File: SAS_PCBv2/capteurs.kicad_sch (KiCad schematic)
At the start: 8 parts, among them J1 BMP280, J12 Conn_01x04, Q4 BS170, Q5 BS170

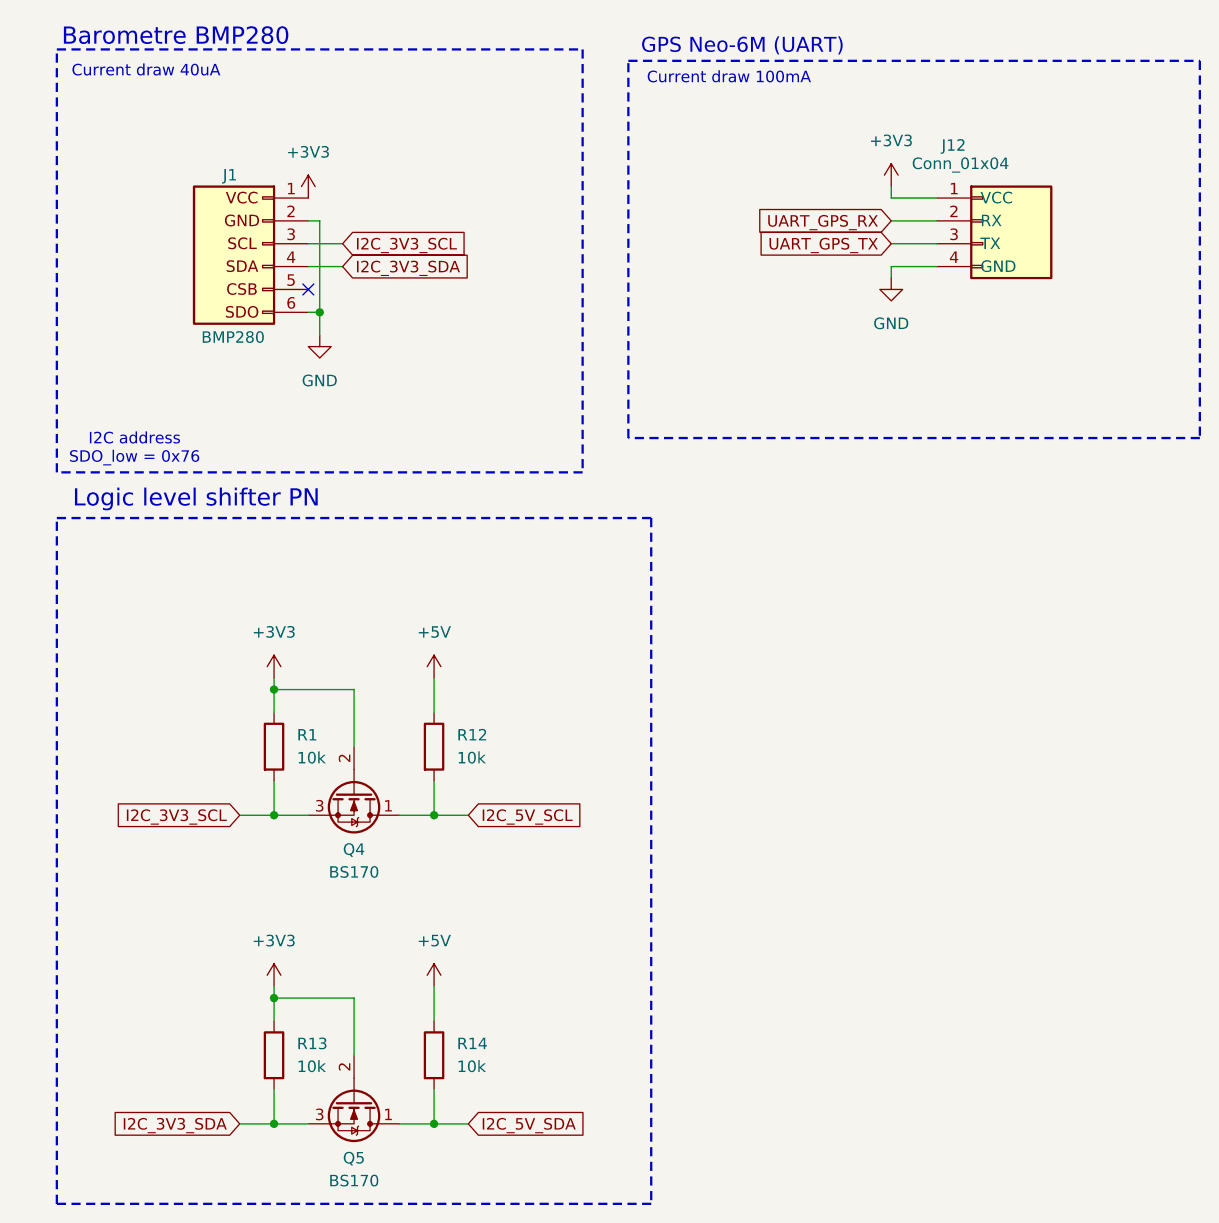
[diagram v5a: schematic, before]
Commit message: Identification des transistors, footprint BMP280 et GPS Neo-6M, correction du fan PWM
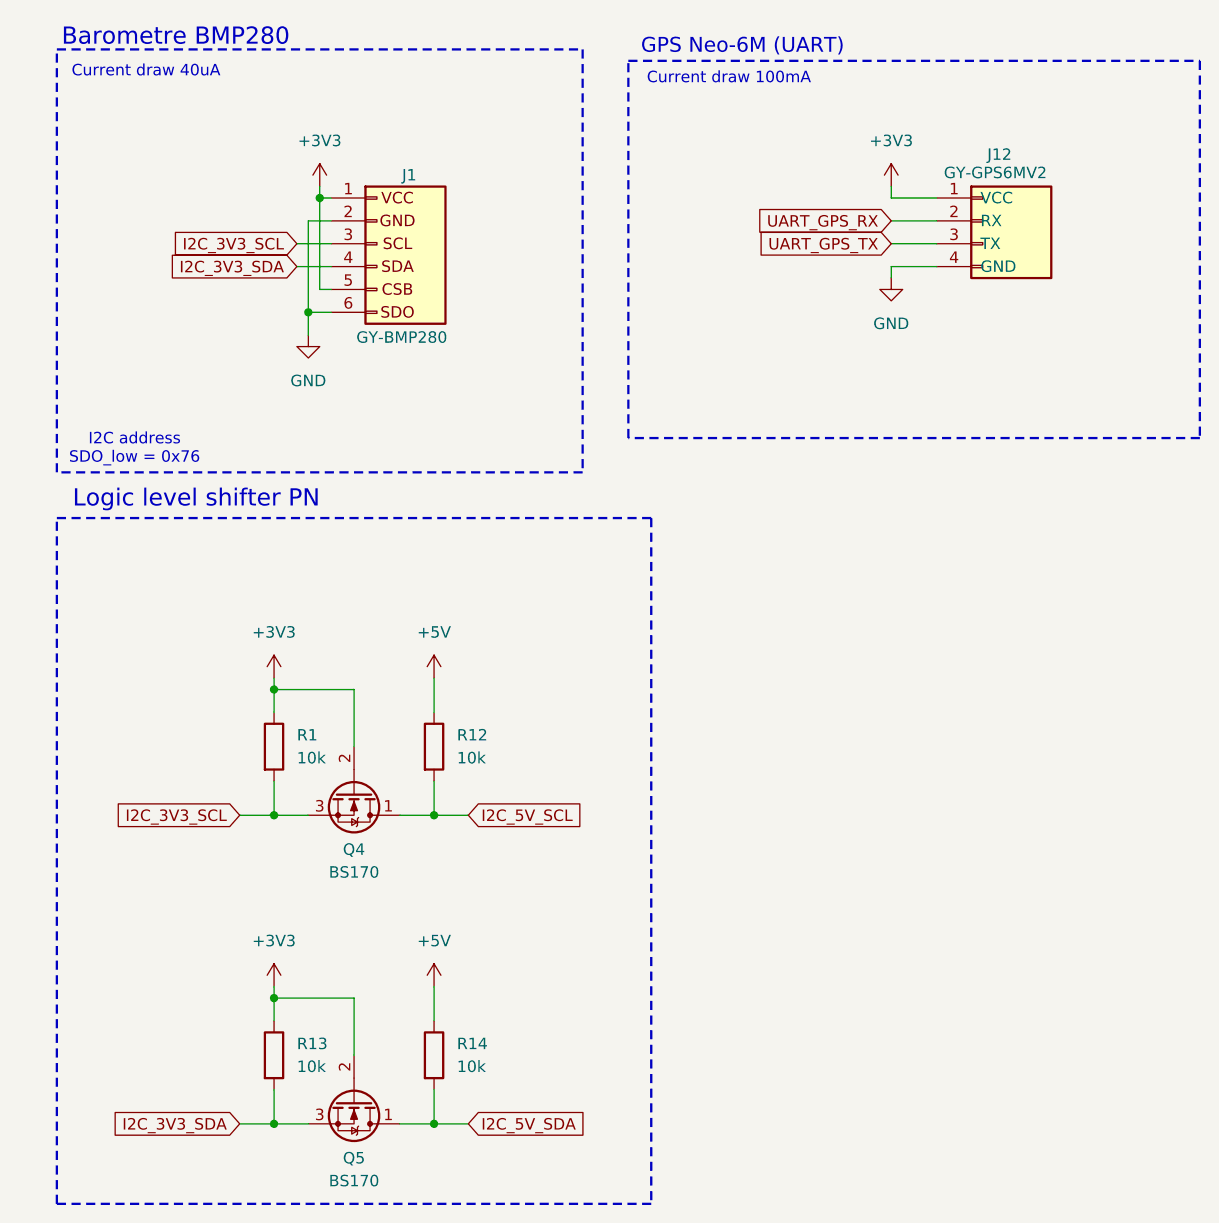
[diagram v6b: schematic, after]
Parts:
- J1: value BMP280 -> GY-BMP280
- J12: value Conn_01x04 -> GY-GPS6MV2
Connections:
- net +3V3: now also J1.5 (Pin_5)
- no-connect marks 1 -> 0
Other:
- moved on the sheet: J1
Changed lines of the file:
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@@
+	)
+	(junction
+		(at 43.18 46.99)
+		(diameter 0)
+		(color 0 0 0 0)
 	)
 	(junction
@@
 	)
 	(junction
+		(at 44.45 34.29)
+		(diameter 0)
+		(color 0 0 0 0)
+	)
+	(junction
 		(at 39.37 123.19)
 		(diameter 0)
@@
 		(color 0 0 0 0)
 	)
-	(junction
-		(at 44.45 46.99)
-		(diameter 0)
-		(color 0 0 0 0)
-	)
-	(no_connect
-		(at 43.18 44.45)
-	)
 	(wire
 		(pts
@@
 	(wire
 		(pts
+			(xy 44.45 34.29) (xy 45.72 34.29)
+		)
+		(stroke
+			(width 0)
+			(type default)
+		)
+	)
+	(wire
+		(pts
 			(xy 48.26 129.54) (xy 48.26 123.19)
 		)
@@
 	(wire
 		(pts
+			(xy 44.45 34.29) (xy 44.45 44.45)
+		)
+		(stroke
+			(width 0)
+			(type default)
+		)
+	)
+	(wire
+		(pts
 			(xy 107.95 39.37) (xy 113.03 39.37)
 		)
@@
 	(wire
 		(pts
-			(xy 43.18 41.91) (xy 46.99 41.91)
+			(xy 45.72 41.91) (xy 41.91 41.91)
 		)
 		(stroke
@@
 	(wire
 		(pts
-			(xy 44.45 46.99) (xy 44.45 49.53)
-		)
-		(stroke
-			(width 0)
-			(type default)
-		)
-	)
-	(wire
-		(pts
-			(xy 44.45 36.83) (xy 43.18 36.83)
+			(xy 43.18 46.99) (xy 43.18 49.53)
+		)
+		(stroke
+			(width 0)
+			(type default)
+		)
+	)
+	(wire
+		(pts
+			(xy 43.18 36.83) (xy 45.72 36.83)
 		)
 		(stroke
@@
 	(wire
 		(pts
+			(xy 45.72 44.45) (xy 44.45 44.45)
+		)
+		(stroke
+			(width 0)
+			(type default)
+		)
+	)
+	(wire
+		(pts
 			(xy 39.37 102.87) (xy 43.18 102.87)
 		)
@@
 	(wire
 		(pts
+			(xy 44.45 33.02) (xy 44.45 34.29)
+		)
+		(stroke
+			(width 0)
+			(type default)
+		)
+	)
+	(wire
+		(pts
 			(xy 39.37 133.35) (xy 39.37 137.16)
 		)
@@
 	(wire
 		(pts
-			(xy 43.18 46.99) (xy 44.45 46.99)
+			(xy 43.18 46.99) (xy 45.72 46.99)
 		)
 		(stroke
@@
 	(wire
 		(pts
-			(xy 44.45 36.83) (xy 44.45 46.99)
+			(xy 43.18 36.83) (xy 43.18 46.99)
 		)
 		(stroke
@@
 	(wire
 		(pts
-			(xy 43.18 39.37) (xy 46.99 39.37)
+			(xy 45.72 39.37) (xy 41.91 39.37)
 		)
 		(stroke
@@
 	(global_label "I2C_3V3_SDA"
 		(shape input)
-		(at 46.99 41.91 0)
+		(at 41.91 41.91 180)
 		(fields_autoplaced yes)
 		(effects
@@
 				(size 1.27 1.27)
 			)
-			(justify left)
+			(justify right)
 		)
 		(property "Intersheetrefs" "${INTERSHEET_REFS}"
-			(at 62.0704 41.91 0)
-			(effects
-				(font
-					(size 1.27 1.27)
-				)
-				(justify left)
+			(at 26.8296 41.91 0)
+			(effects
+				(font
+					(size 1.27 1.27)
+				)
+				(justify right)
 				(hide yes)
 			)
@@
 	(global_label "I2C_3V3_SCL"
 		(shape input)
-		(at 46.99 39.37 0)
+		(at 41.91 39.37 180)
 		(fields_autoplaced yes)
 		(effects
@@
 				(size 1.27 1.27)
 			)
-			(justify left)
+			(justify right)
 		)
 		(property "Intersheetrefs" "${INTERSHEET_REFS}"
-			(at 62.0099 39.37 0)
-			(effects
-				(font
-					(size 1.27 1.27)
-				)
-				(justify left)
+			(at 26.8901 39.37 0)
+			(effects
+				(font
+					(size 1.27 1.27)
+				)
+				(justify right)
 				(hide yes)
 			)
@@
 		(dnp no)
 		(property "Reference" "J12"
-			(at 113.538 28.448 0)
+			(at 118.618 29.464 0)
 			(effects
 				(font
@@
 			)
 		)
-		(property "Value" "Conn_01x04"
-			(at 110.236 30.48 0)
+		(property "Value" "GY-GPS6MV2"
+			(at 113.792 31.496 0)
 			(effects
 				(font
@@
 			)
 		)
-		(property "Datasheet" "~"
+		(property "Datasheet" "https://components101.com/sites/default/files/component_datasheet/NEO6MV2%20GPS%20Module%20Datasheet.pdf"
 			(at 118.11 36.83 0)
 			(effects
@@
 			)
 		)
-		(property "Description" "Generic connector, single row, 01x04, script generated (kicad-library-utils/schlib/autogen/connector/)"
+		(property "Description" "Header NEO-6M"
 			(at 118.11 36.83 0)
 			(effects
@@
 	(symbol
 		(lib_id "Connector_Generic:Conn_01x06")
-		(at 38.1 39.37 0)
-		(mirror y)
+		(at 50.8 39.37 0)
 		(unit 1)
 		(exclude_from_sim no)
@@
 		(dnp no)
 		(property "Reference" "J1"
-			(at 35.306 31.75 0)
+			(at 53.594 31.75 0)
 			(effects
 				(font
@@
 			)
 		)
-		(property "Value" "BMP280"
-			(at 38.354 49.784 0)
+		(property "Value" "GY-BMP280"
+			(at 48.514 49.784 0)
 			(effects
 				(font
@@
 		)
 		(property "Footprint" "Connector_PinHeader_2.54mm:PinHeader_1x06_P2.54mm_Vertical"
-			(at 38.1 39.37 0)
+			(at 50.8 39.37 0)
 			(effects
 				(font
@@
 		)
 		(property "Datasheet" "https://www.bosch-sensortec.com/media/boschsensortec/downloads/datasheets/bst-bmp280-ds001.pdf"
-			(at 38.1 39.37 0)
+			(at 50.8 39.37 0)
 			(effects
 				(font
@@
 		)
 		(property "Description" "Barometre"
-			(at 38.1 39.37 0)
+			(at 50.8 39.37 0)
 			(effects
 				(font
@@
 		)
 		(property "AVAILABILITY" ""
-			(at 38.1 39.37 0)
+			(at 50.8 39.37 0)
 			(effects
 				(font
@@
 		)
 		(property "Digikey" ""
-			(at 38.1 39.37 0)
+			(at 50.8 39.37 0)
 			(effects
 				(font
@@
 		)
 		(property "MF" ""
-			(at 38.1 39.37 0)
+			(at 50.8 39.37 0)
 			(effects
 				(font
@@
 		)
 		(property "MP" ""
-			(at 38.1 39.37 0)
+			(at 50.8 39.37 0)
 			(effects
 				(font
@@
 		)
 		(property "PACKAGE" ""
-			(at 38.1 39.37 0)
+			(at 50.8 39.37 0)
 			(effects
 				(font
@@
 		)
 		(property "PRICE" ""
-			(at 38.1 39.37 0)
+			(at 50.8 39.37 0)
 			(effects
 				(font
@@
 		)
 		(property "PURCHASE-URL" ""
-			(at 38.1 39.37 0)
+			(at 50.8 39.37 0)
 			(effects
 				(font
@@
 	(symbol
 		(lib_id "power:+3V3")
-		(at 43.18 34.29 0)
+		(at 44.45 33.02 0)
+		(mirror y)
 		(unit 1)
 		(exclude_from_sim no)
@@
 		(fields_autoplaced yes)
 		(property "Reference" "#PWR01"
-			(at 43.18 38.1 0)
+			(at 44.45 36.83 0)
 			(effects
 				(font
@@
 		)
 		(property "Value" "+3V3"
-			(at 43.18 29.21 0)
+			(at 44.45 27.94 0)
 			(effects
 				(font
@@
 		)
 		(property "Footprint" ""
-			(at 43.18 34.29 0)
+			(at 44.45 33.02 0)
 			(effects
 				(font
@@
 		)
 		(property "Datasheet" ""
-			(at 43.18 34.29 0)
+			(at 44.45 33.02 0)
 			(effects
 				(font
@@
 		)
 		(property "Description" "Power symbol creates a global label with name \"+3V3\""
-			(at 43.18 34.29 0)
+			(at 44.45 33.02 0)
 			(effects
 				(font
@@
 			)
 		)
-		(property "Datasheet" "https://www.onsemi.com/pub/Collateral/BS170-D.PDF"
+		(property "Datasheet" "https://www.onsemi.com/pdf/datasheet/mmbf170-d.pdf"
 			(at 44.45 139.7 0)
 			(effects
@@
 			)
 		)
-		(property "Datasheet" "https://www.onsemi.com/pub/Collateral/BS170-D.PDF"
+		(property "Datasheet" "https://www.onsemi.com/pdf/datasheet/mmbf170-d.pdf"
 			(at 44.45 105.41 0)
 			(effects
@@
 	(symbol
 		(lib_id "power:GND")
-		(at 44.45 49.53 0)
+		(at 43.18 49.53 0)
+		(mirror y)
 		(unit 1)
 		(exclude_from_sim no)
@@
 		(fields_autoplaced yes)
 		(property "Reference" "#PWR02"
-			(at 44.45 55.88 0)
+			(at 43.18 55.88 0)
 			(effects
 				(font
@@
 		)
 		(property "Value" "GND"
-			(at 44.45 54.61 0)
+			(at 43.18 54.61 0)
 			(effects
 				(font
@@
 		)
 		(property "Footprint" ""
-			(at 44.45 49.53 0)
+			(at 43.18 49.53 0)
 			(effects
 				(font
@@
 		)
 		(property "Datasheet" ""
-			(at 44.45 49.53 0)
+			(at 43.18 49.53 0)
 			(effects
 				(font
@@
 		)
 		(property "Description" "Power symbol creates a global label with name \"GND\" , ground"
-			(at 44.45 49.53 0)
-			(effects
-				(font
+			(at 43.18 49.53 0)
+			(effects
+				(font

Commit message: Ajout du connecteur spécial pour les radios, insertion des footprints dans le PCB, fin du schéma
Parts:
- R1, R12, R13, R14: footprint (none) -> Resistor_THT:R_Axial_DIN0207_L6.3mm_D2.5mm_P10.16mm_Horizontal; Digikey (none) -> MFR-25FRF52-10K
